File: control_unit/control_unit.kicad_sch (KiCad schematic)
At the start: 113 parts, among them J2 Conn_01x02_Socket, J4 SERVO_PWM, J5 BLDC1, J6 BLDC1, J7 BLDC1, J8 BLDC1, J9 Barrel_Jack_Switch, M1 Motor_Servo, M2 Fan, Q3 2N7002, Q4 MMBT5551L, Q7 AO3400A, Q8 AO3400A, U1 CL6808, U14 MCP2515-xSO, U15 BNO055 DIP, U3 ATA6561-GAQW-N, U4 ADS1015IDGS, X1 16MHz

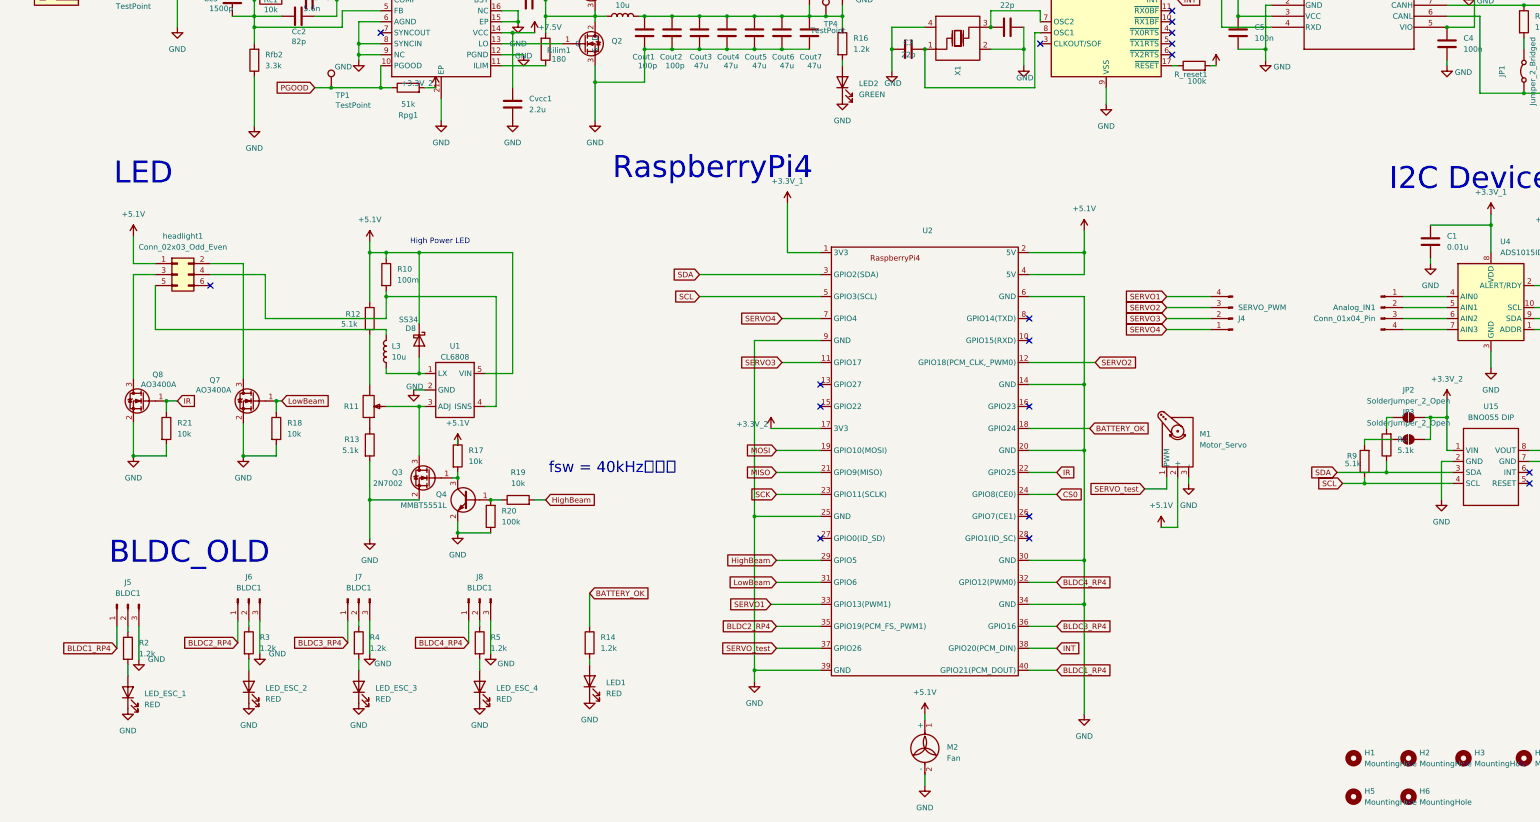
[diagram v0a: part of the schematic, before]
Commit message: 基板防水(LAN)作成開始
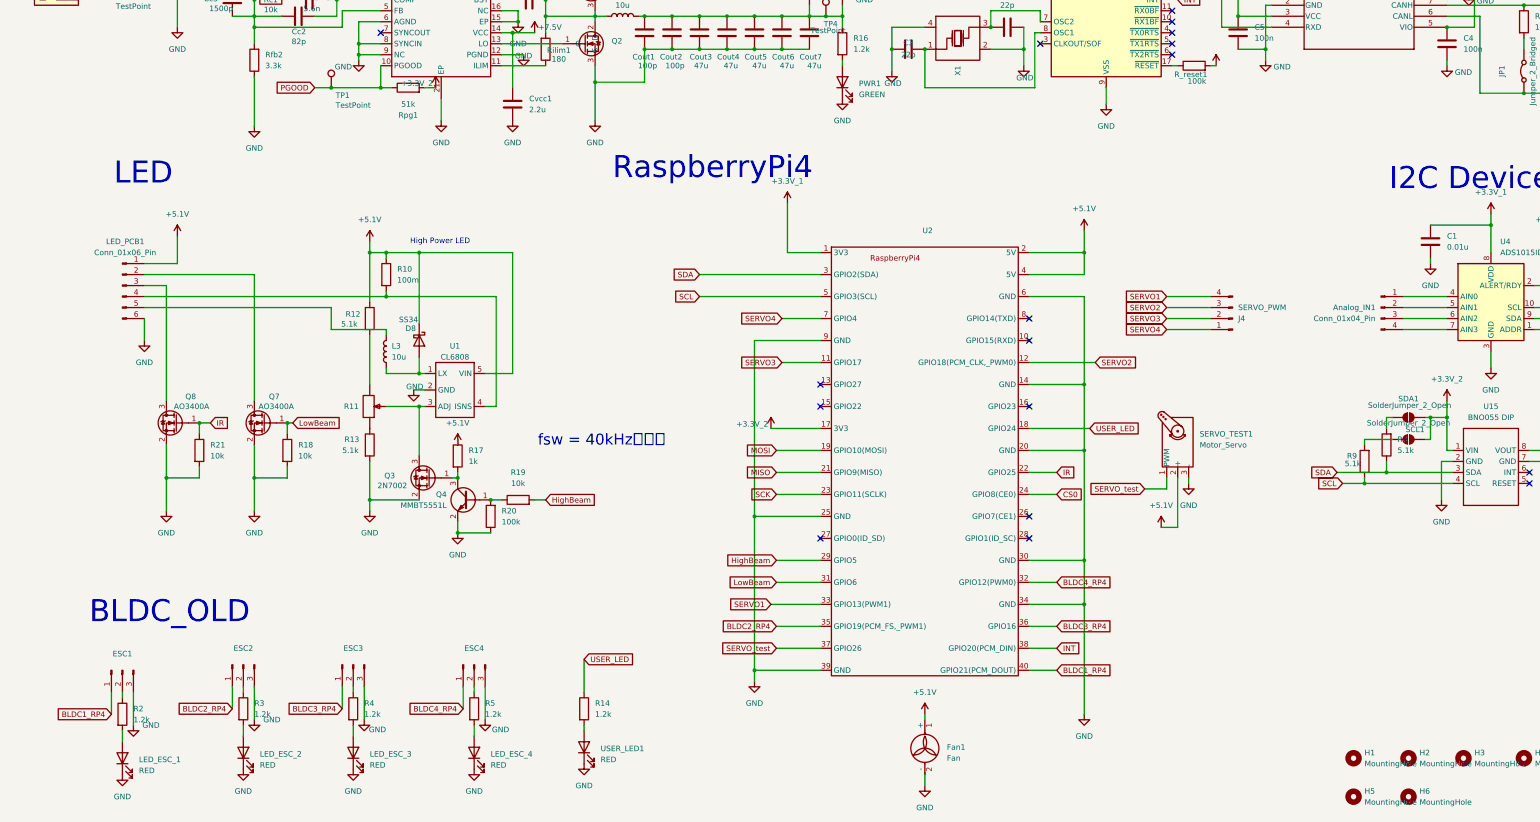
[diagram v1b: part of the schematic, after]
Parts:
- removed headlight1: Conn_02x03_Odd_Even, Connector_PinHeader_2.54mm:PinHeader_2x03_P2.54mm_Vertical, symbol Connector_Generic:Conn_02x03_Odd_Even
- added LED_PCB1: Conn_01x06_Pin, Connector_JST:JST_XA_B06B-XASK-1_1x06_P2.50mm_Vertical, symbol Connector:Conn_01x06_Pin
- ESC1: renamed from J5; value BLDC1 -> ~
- ESC2: renamed from J6; value BLDC1 -> ~
- ESC3: renamed from J7; value BLDC1 -> ~
- ESC4: renamed from J8; value BLDC1 -> ~
- R17: value 10k -> 1k
- TP1, TP2, TP4: footprint Connector_Pin:Pin_D0.7mm_L6.5mm_W1.8mm_FlatFork -> Connector_Pin:Pin_D1.0mm_L10.0mm
- renumbered M2 to Fan1, LED2 to PWR1, JP3 to SCL1, JP2 to SDA1, M1 to SERVO_TEST1, LED1 to USER_LED1
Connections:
- net +5.1V: now also LED_PCB1.1 (Pin_1)
- net GND: now also LED_PCB1.6 (Pin_6)
- net at Q8.3 (D): now also LED_PCB1.3 (Pin_3)
- net at L3.2: now also LED_PCB1.5 (Pin_5)
- net at R10.2, U1.4 (ISNS): now also LED_PCB1.4 (Pin_4)
- net at Q7.3 (D): now also LED_PCB1.2 (Pin_2)
- net BATTERY_OK renamed USER_LED
- no-connect marks 18 -> 17
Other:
- moved on the sheet: ESC1, ESC2, ESC3, ESC4, LED_ESC_1, LED_ESC_2, LED_ESC_3, LED_ESC_4, Q7, Q8, R14, R18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

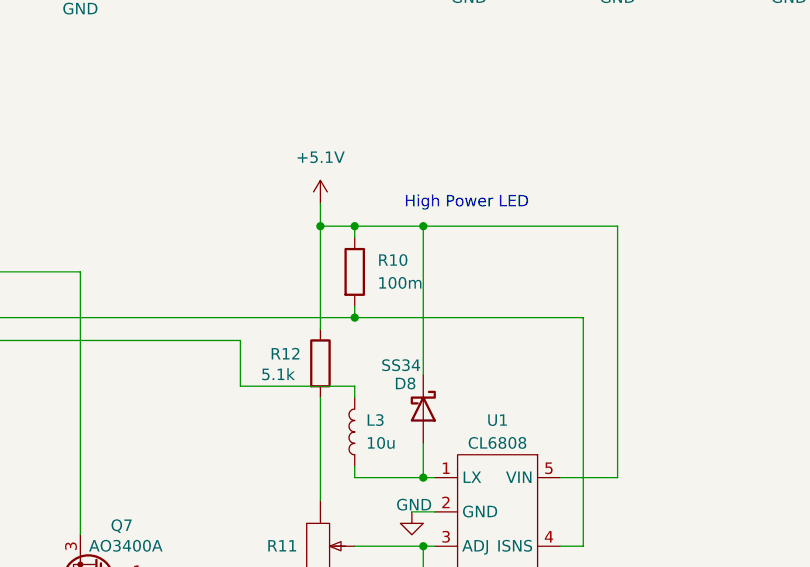
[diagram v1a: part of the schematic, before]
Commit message: 基板防水REV00発注完了
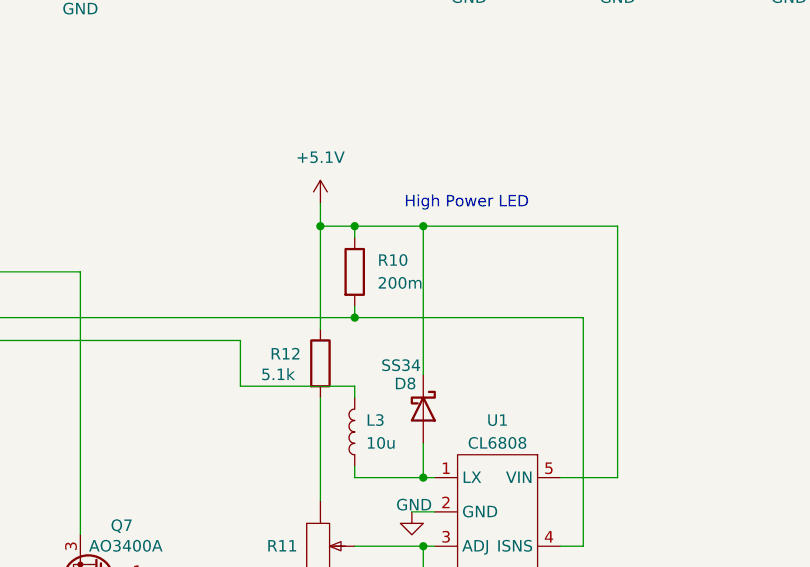
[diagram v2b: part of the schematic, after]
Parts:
- R10: value 100m -> 200m
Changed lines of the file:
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@@
 			)
 		)
-		(property "Value" "100m"
+		(property "Value" "200m"
 			(at 102.87 121.9199 0)
 			(effects

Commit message: 制御基板REV01完成
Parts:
- removed D2: SS54, basic_parts:SMA_L4.4-W2.8-LS5.4-R-RD, symbol basic_parts:SS54_C22452
- removed Q4: MMBT5551L, Package_TO_SOT_SMD:SOT-23, symbol Transistor_BJT:MMBT5551L
- removed R1: 20m, Diode_SMD:D_2010_5025Metric_Pad1.52x2.65mm_HandSolder, symbol Device:R
- removed R16: 1.2k, Resistor_SMD:R_0603_1608Metric, symbol Device:R
- removed R19: 10k, Resistor_SMD:R_0603_1608Metric, symbol Device:R
- removed SCL1, SDA1: SolderJumper_2_Open, Jumper:SolderJumper-2_P1.3mm_Open_RoundedPad1.0x1.5mm, symbol Jumper:SolderJumper_2_Open
- removed TP1: TestPoint, Connector_Pin:Pin_D1.0mm_L10.0mm, symbol Connector:TestPoint
- removed U15: BNO055 DIP, myfootprint:BNO055 DIP, symbol MyLibrary:BNO055 DIP
- removed U5: ~, basic_parts:VQFN-20_L4.5-W3.5-P0.50-BL-EP, symbol basic_parts:LM25145RGYR
- added D1: SS36, Diode_SMD:D_SMA, symbol Diode:SS36
- added JP1, JP2: SolderJumper_2_Bridged, Jumper:SolderJumper-2_P1.3mm_Bridged_RoundedPad1.0x1.5mm, symbol Jumper:SolderJumper_2_Bridged
- added Q3, Q5: 2N7002, Package_TO_SOT_SMD:SOT-23, symbol Transistor_FET:2N7002
- added R15, R2, R3, R4, R5: 100m, Resistor_SMD:R_1206_3216Metric, symbol Device:R
- added R9: 1.2k, Resistor_SMD:R_0603_1608Metric_Pad0.98x0.95mm_HandSolder, symbol Device:R
- added U1: ~, specific_footprint_library:VQFN-20_L4.5-W3.5-P0.50-BL-EP, symbol specific_library:LM5146RGYR
- added U7: BNO055 DIP, specific_footprint_library:BNO055 DIP, symbol specific_library:BNO055 DIP
- Cc1: renamed from Cc3; value 1500p -> 2.2n; LCSC (none) -> C1604
- Cc2: value 82p -> 12p; LCSC (none) -> C38523
- Cc3: renamed from Cc1; value 5.6n -> 3.3n; LCSC (none) -> C1613
- Cin1, Cin10, Cin11, Cin12, Cin2, Cin3, Cin4, Cin5, Cin6, Cin7, Cin8, Cin9: LCSC C97973 -> C126612
- L1: renamed from L3; footprint basic_parts:IND-SMD_L13.8-W12.6 -> specific_footprint_library:IND-SMD_L13.8-W12.6
- L2: footprint basic_parts:IND-SMD_L13.8-W12.6 -> specific_footprint_library:IND-SMD_L13.8-W12.6
- LED1: renamed from PWR1; value GREEN -> Emerald
- LED_PCB1: footprint Connector_JST:JST_XA_B06B-XASK-1_1x06_P2.50mm_Vertical -> Connector_JST:JST_XA_B06B-XASK-1-A_1x06_P2.50mm_Vertical
- R11: renamed from R12; value 5.1k -> 13k; LCSC C23186 -> C22797
- R12: renamed from R13; value 5.1k -> 3k; LCSC C23186 -> C4211
- R14: renamed from R10; value 200m -> 100m
- R16: renamed from R17; value 1k -> 10k
- R18: renamed from R20; value 100k -> 10k; LCSC C25803 -> C25804
- Rc1: renamed from Rc2; value 560 -> 470; LCSC C23204 -> C23179
- Rc2: renamed from Rc1; value 10k -> 13k; LCSC C25804 -> C22797
- Rilim1: LCSC C8218 -> C22828
- U3: renamed from U2; footprint basic_parts:Raspberry Pi 4 hat -> specific_footprint_library:RaspberryPi4 hat
- USER_LED1: value RED -> YELLOW
- X1: footprint basic_parts:OSC-SMD_4P-L3.2-W2.5-BL -> specific_footprint_library:OSC-SMD_4P-L3.2-W2.5-BL
- renumbered C3 to C1, C5 to C3, C1 to C4, C4 to C5, D8 to D2, H5 to H2, H2 to H3, H6 to H4, H3 to H5, H4 to H6, J9 to J1, J4 to J3, Analog_IN1 to J4, CAN1 to J5, CAN2 to J6, JP1 to JP3, Q8 to Q1, Q7 to Q2, Q3 to Q4, Q1 to Q6, Q2 to Q7, R2 to R1, R4 to R10, R11 to R13, R5 to R17, R14 to R19, R9 to R20, R8 to R21, R7 to R22, R6 to R23, R15 to R24, R21 to R6, R3 to R7, R18 to R8, TP2 to TP1, TP4 to TP2, U1 to U2, U14 to U4, U3 to U5, U4 to U6
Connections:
- net +24V: now also R2.2, R3.2, R4.2, R5.2, U1.20 (VIN)
- net +3.3V_2: now also JP1.2 (B), JP2.2 (B), U7.1 (VIN); no longer Rpg1.2
- net +5.1V: now also Rpg1.2, R9.2
- net +7.5V: now also U1.14 (VCC)
- net GND: now also Q3.3 (D), Q5.2 (S), U1.12 (PGND), U1.15 (EP), U1.16 (NC), U1.21 (EP), U1.6 (AGND), U1.8 (SYNCIN), U1.9 (NC), U7.2 (GND), U7.7 (GND); no longer LED1.1 (K)
- net HighBeam: now also R18.2, Q5.1 (G)
- net SCL: now also U7.4 (SCL)
- net SDA: now also U7.3 (SDA)
- net at Q6.1 (G): now also U1.18 (HO)
- net at Cbst1.2, L2.1, Q6.3 (S)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: now also U1.19 (SW)
- net at R21.2: now also JP1.1 (A)
- net at Q4.1 (G), R16.2: now also Q5.3 (D)
- net at LED_PCB1.4 (Pin_4), U2.4 (ISNS): now also R15.2; no longer R14.2
- net at Rilim1.1: now also U1.11 (ILIM)
- net at R24.1: now also U7.8 (VOUT)
- net at Cc1.2, Cc2.1, Rc2.2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: now also U1.5 (FB)
- net at LED1.2 (A): now also R9.1
- net at Cc2.2, Cc3.2: now also U1.4 (COMP)
- net at R20.2: now also JP2.1 (A)
- net at Ruv1.2, Ruv2.1: now also U1.1 (EN/UVLO)
- net at J1.1, J2.1 (Pin_1): now also D1.2 (A)
- net at Q7.1 (G): now also U1.13 (LO)
- net at Cbst1.1: now also U1.17 (BST)
- net at Css1.2: now also U1.3 (SS/TRK)
- net at Rt1.2: now also U1.2 (RT)
- net BLDC1_RP4 renamed ESC1_RP4
- net BLDC2_RP4 renamed ESC2_RP4
- net BLDC3_RP4 renamed ESC3_RP4
- net BLDC4_RP4 renamed ESC4_RP4
- net PGOOD: no longer names the net of Rpg1.1
- net PGOOD: now also Q3.1 (G), U1.10 (PGOOD)
- new net: D1.1 (K), R2.1, R3.1, R4.1, R5.1
- new net: R14.2, R15.1
- new net: LED1.1 (K), Q3.2 (S)
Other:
- note added: "DCR=20m"
- note added: "ESC1 GPIO21 ESC2 GPIO19 ESC3 GPIO16 ESC4 GPIO12"
- note added: "ESC_OLD"
- note added: "HighBeam GPIO5 LowBeam GPIO6 IR GPIO25"
- note added: "Iled = (5.1V - 2.8V) / 1.2k = 1.92mA"
- note added: "Rated Voltage = 100V"
- note added: "Rated Voltage = 50V"
- note added: "Rated Voltage = 60V"
- note added: "Vadj = 0.59 ~ 2.55V"
- note added: "Vin_on=8.7V"
- note removed: "BLDC_OLD"
- moved on the sheet: ESC1, Fan1, J3, LED1, LED_ESC_1, R1, R14, R19, Rpg1, SERVO_TEST1, U3, USER_LED1
